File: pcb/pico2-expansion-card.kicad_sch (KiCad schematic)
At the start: 37 parts, among them J3 Conn_01x04_Socket, J4 Conn_01x03_Socket, P1 USB_C_Plug_USB2.0, SW1 SW_Push, U2 RP2354A, U4 AP2127K-3.3, Y1 ABM8-272-T3

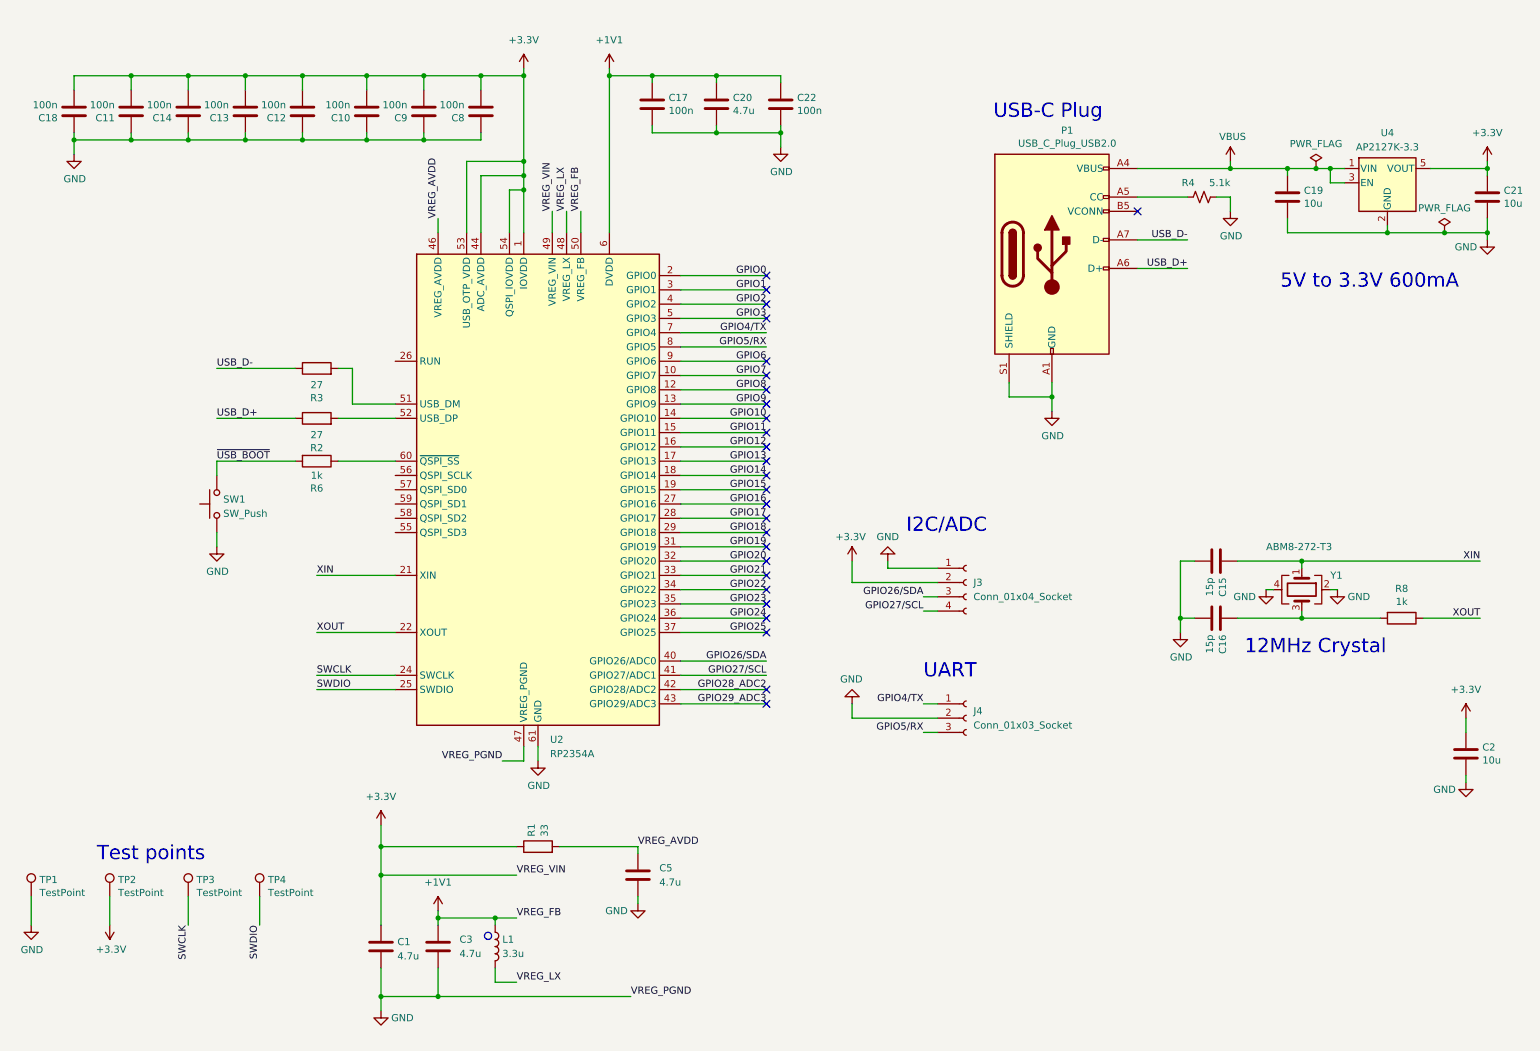
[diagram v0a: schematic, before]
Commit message: edit schematic, change type-c, add single button bootsel reset, make pcb
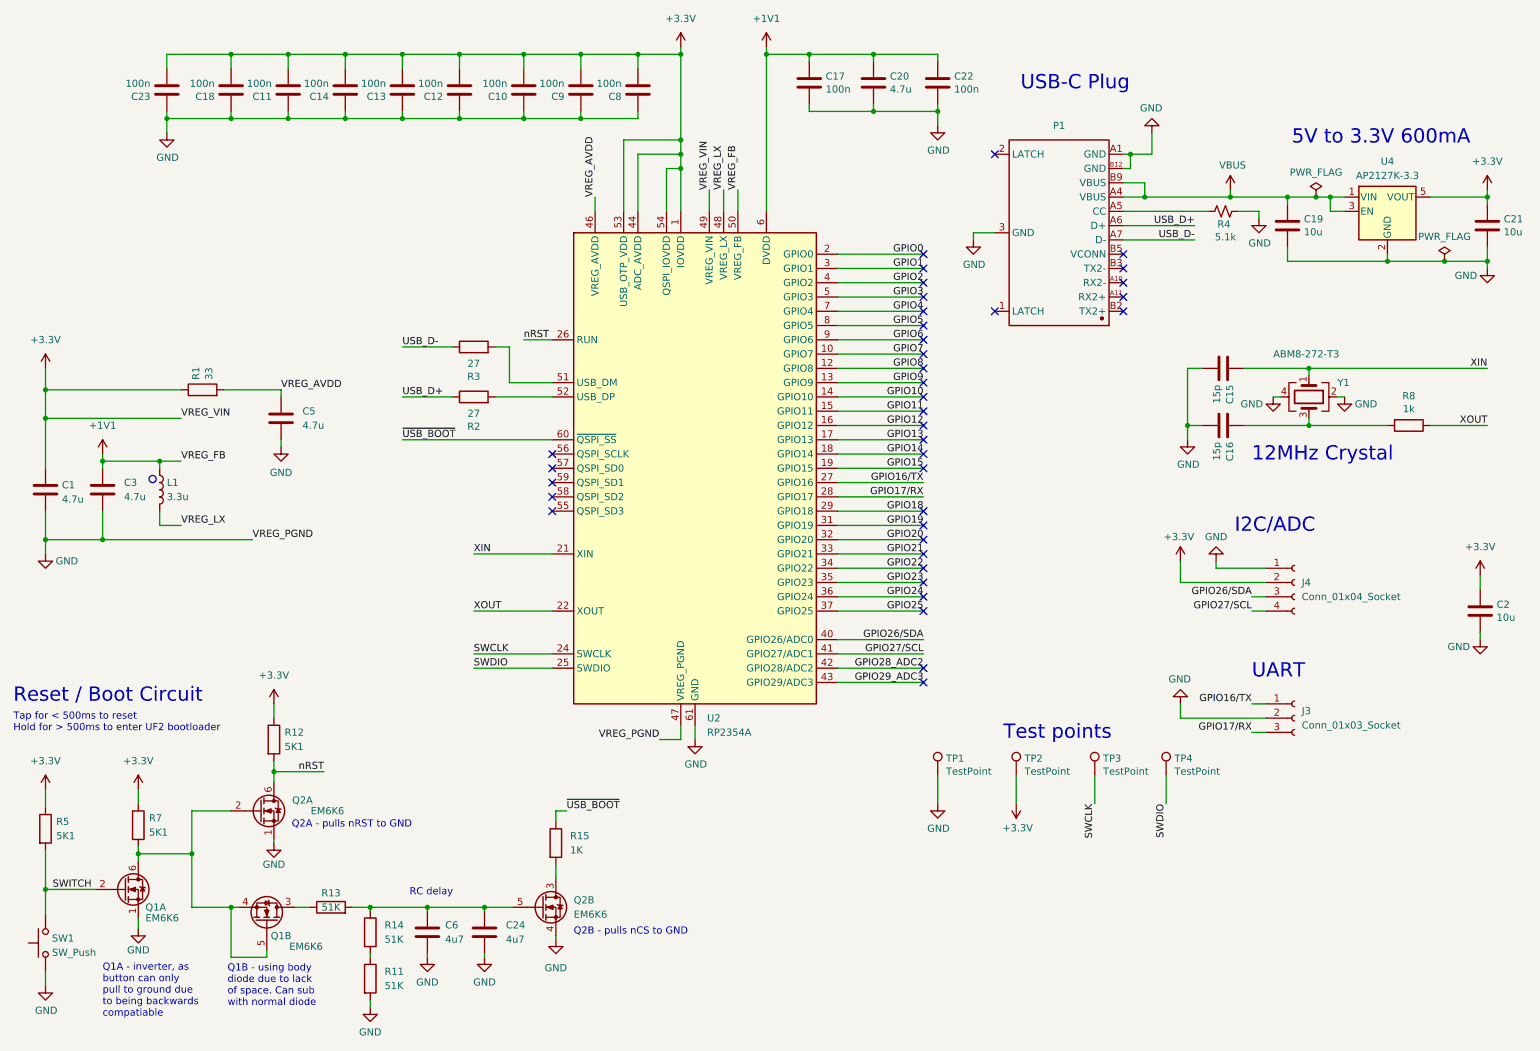
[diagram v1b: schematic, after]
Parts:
- removed P1: USB_C_Plug_USB2.0, pico2parts:USB-SMD_TC-002_1, symbol Connector:USB_C_Plug_USB2.0
- removed R6: 1k, Resistor_SMD:R_0402_1005Metric, symbol Device:R
- added C23: 100n, Capacitor_SMD:C_0402_1005Metric, symbol Device:C
- added C24, C6: 4u7, Capacitor_SMD:C_0402_1005Metric, symbol Device:C
- added P1: (no value), pico2parts:USB-C-SMD_TYPE-C-31-G-10, symbol pico2symbols:TYPE-C-31-G-10
- added Q1, Q2: EM6K6, Package_TO_SOT_SMD:SOT-563, symbol Transistor_FET:FDG6335N
- added R11, R13, R14: 51K, Resistor_SMD:R_0402_1005Metric, symbol Device:R
- added R12, R5, R7: 5K1, Resistor_SMD:R_0402_1005Metric, symbol Device:R
- added R15: 1K, Resistor_SMD:R_0402_1005Metric, symbol Device:R
- C1, C3: footprint Capacitor_SMD:C_0402_1005Metric -> pico2parts:C_0402_1005Metric_small_pads
- J3: renamed from J4; footprint Connector_JST:JST_SH_BM03B-SRSS-TB_1x03-1MP_P1.00mm_Vertical -> Connector_JST:JST_SH_SM03B-SRSS-TB_1x03-1MP_P1.00mm_Horizontal
- J4: renamed from J3; footprint Connector_JST:JST_SH_BM04B-SRSS-TB_1x04-1MP_P1.00mm_Vertical -> Connector_JST:JST_SH_SM04B-SRSS-TB_1x04-1MP_P1.00mm_Horizontal
- U2: footprint Package_DFN_QFN:QFN-60-1EP_7x7mm_P0.4mm_EP3.4x3.4mm -> pico2parts:RP2350-QFN-60-1EP_7x7_P0.4mm_EP3.4x3.4mm_ThermalVias
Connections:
- net +3.3V: now also C23.2, R12.1, R5.1, R7.1
- net GND: now also C23.1, C24.2, C6.2, P1.3 (GND), P1.A1 (GND), P1.B12 (GND), Q1.1 (S), Q2.1 (S), Q2.4 (S), R11.2
- net USB_D+: now also P1.A6 (D+)
- net USB_D-: now also P1.A7 (D-)
- net VBUS: now also P1.A4 (VBUS), P1.B9 (VBUS)
- net ~{USB_BOOT}: now also U2.60 (~{QSPI_SS}), R15.1; no longer SW1.2
- net at R4.1: now also P1.A5 (CC)
- net nRST: now reaches U2.26 (RUN)
- net nRST: now also Q2.6 (D), R12.2
- net GPIO16 renamed GPIO16/TX
- net GPIO16/TX: now also J3.1 (Pin_1)
- net GPIO17 renamed GPIO17/RX
- net GPIO17/RX: now also J3.3 (Pin_3)
- net GPIO4/TX renamed GPIO4
- net GPIO4: no longer J3.1 (Pin_1)
- net GPIO5/RX renamed GPIO5
- net GPIO5: no longer J3.3 (Pin_3)
- new net: Q1.4 (S), Q1.5 (G), Q1.6 (D), Q2.2 (G), R7.2
- new net: C24.1, C6.1, Q2.5 (G), R13.2, R14.1
- new net: R11.1, R14.2
- new net: Q1.3 (D), R13.1
- new net: Q2.3 (D), R15.2
- new net SWITCH: Q1.2 (G), R5.2, SW1.2
- no-connect marks 27 -> 38
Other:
- note added: "Q1A - inverter, as button can only pull to ground due to being backwards compatiable"
- note added: "Q1B - using body diode due to lack of space. Can sub with normal diode"
- note added: "Q2A - pulls nRST to GND"
- note added: "Q2B - pulls nCS to GND"
- note added: "RC delay"
- note added: "Reset / Boot Circuit"
- note added: "Tap for < 500ms to reset Hold for > 500ms to enter UF2 bootloader"
- company: (none) -> Riscfruit Laboratory
- moved on the sheet: C1, C10, C11, C12, C13, C14, C15, C16, C17, C18, C19, C2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

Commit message: cosmetic minor changes
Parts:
- removed P1: (no value), pico2parts:USB-C-SMD_TYPE-C-31-G-10, symbol pico2symbols:TYPE-C-31-G-10
- added P1: (no value), symbol pico2symbols:korean_type-c_top_mount
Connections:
- net GND: now also P1.3 (GND), P1.A1 (GND), P1.B12 (GND)
- net USB_D+: now also P1.A6 (D+)
- net USB_D-: now also P1.A7 (D-)
- net VBUS: now also P1.A4 (VBUS), P1.B9 (VBUS)
- net at R4.1: now also P1.A5 (CC)
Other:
- moved on the sheet: C1, C10, C11, C12, C13, C14, C17, C18, C20, C22, C23, C3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

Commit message: fix missing i2c pull up
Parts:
- added R6, R9: 10K, Resistor_SMD:R_0402_1005Metric, symbol Device:R
- P1: footprint (none) -> pico2parts:USB-C-SMD_TYPE-C-31-G-10
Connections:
- net +3.3V: now also R6.1, R9.1
- net GPIO26/SDA: now also R6.2
- net GPIO27/SCL: now also R9.2
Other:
- moved on the sheet: C1, C15, C16, C3, C5, J3, J4, L1, R1, R8, TP1, TP2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

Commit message: fix false UART
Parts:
- removed J3: Conn_01x03_Socket, Connector_JST:JST_SH_SM03B-SRSS-TB_1x03-1MP_P1.00mm_Horizontal, symbol Connector:Conn_01x03_Socket
- added J3: Conn_01x04_Socket, Connector_JST:JST_SH_SM04B-SRSS-TB_1x04-1MP_P1.00mm_Horizontal, symbol Connector:Conn_01x04_Socket
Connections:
- net +3.3V: now also J3.2 (Pin_2)
- net GND: now also J3.1 (Pin_1)
- net GPIO16/TX: now also J3.3 (Pin_3)
- net GPIO17/RX: now also J3.4 (Pin_4)
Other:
- moved on the sheet: TP1, TP2, TP3, TP4
